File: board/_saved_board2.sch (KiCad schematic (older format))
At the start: 71 parts, among them J1 Battery, J2 Conn_01x06_Male, J3 Conn_ARM_JTAG_SWD_10, J4 Range_Front, J5 Range_Left, J6 Range_Right, J7 Battery, SW1 RST, SW2 SW_Push, SW3 SW_Push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

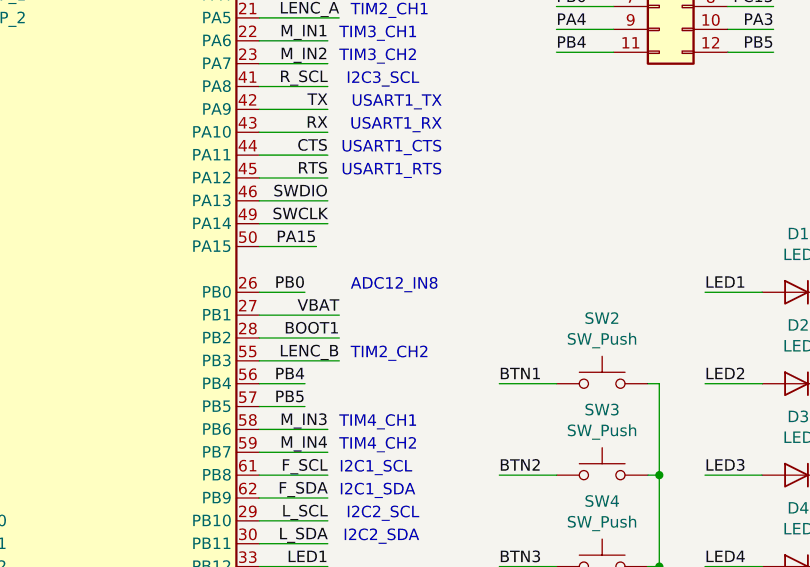
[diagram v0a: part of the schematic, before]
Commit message: Label the adc channel for battery voltage
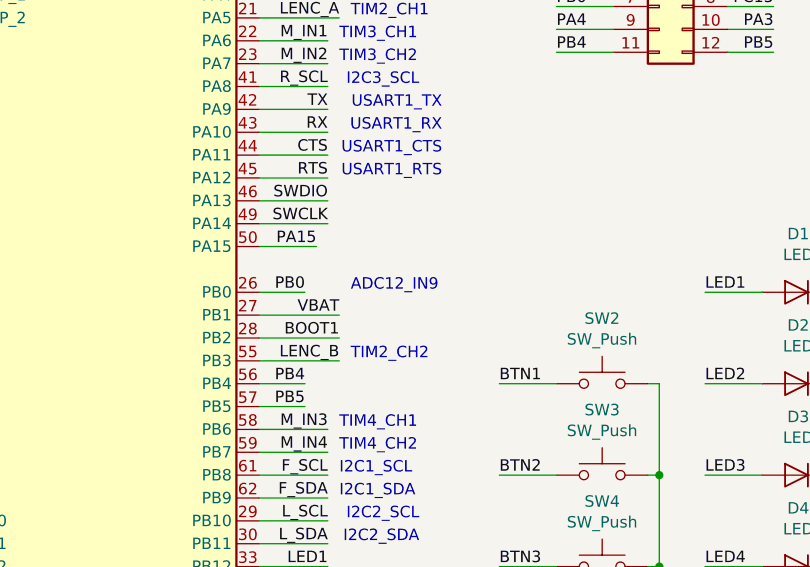
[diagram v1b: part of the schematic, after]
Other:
- note added: "ADC12_IN9"
- note removed: "ADC12_IN8"
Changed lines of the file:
@@
 $EndComp
 Text Notes 6950 4500 0    50   ~ 0
-ADC12_IN8
+ADC12_IN9
 $EndSCHEMATC
